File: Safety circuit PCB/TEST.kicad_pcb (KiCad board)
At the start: 2 copper layers, 100 x 50 mm, 30 parts, among them J1 430450801, J2 430450801, Q1 2N7002K, Q2 2N7002K, Q3 2N7002K, Q4 2N7002K, Q5 2N7002K, Q6 2N7002K, Q7 2N7002K

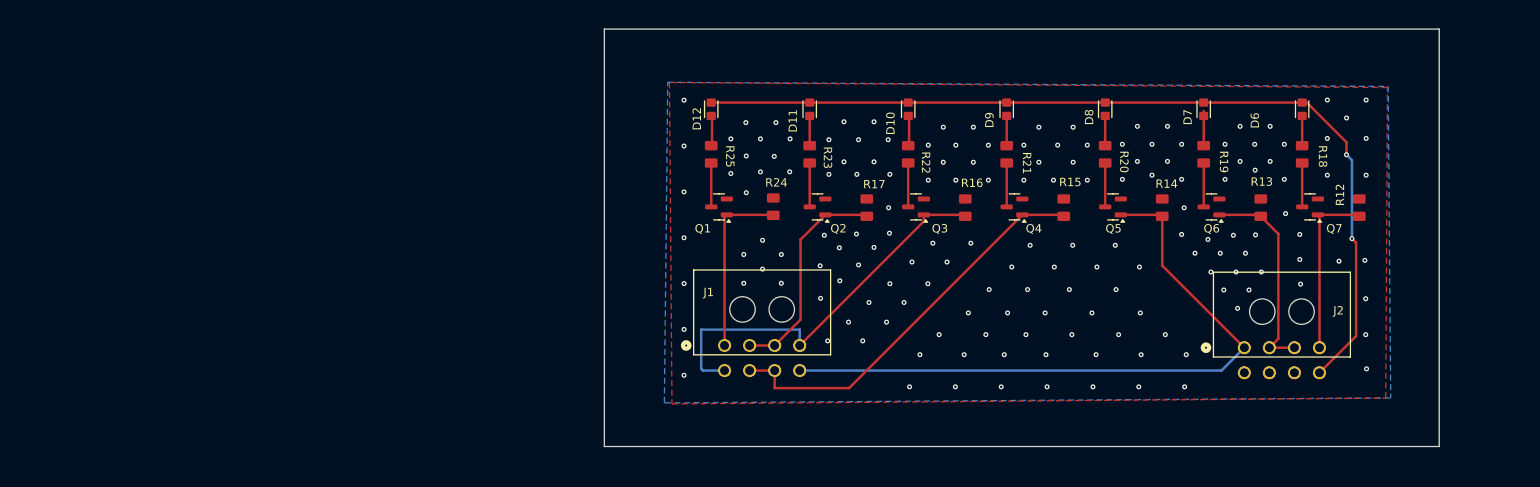
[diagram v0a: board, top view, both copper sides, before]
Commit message: Flip connectors, make more sane pin assignments for connections, get nicer tracks, and make dimensions reasonable
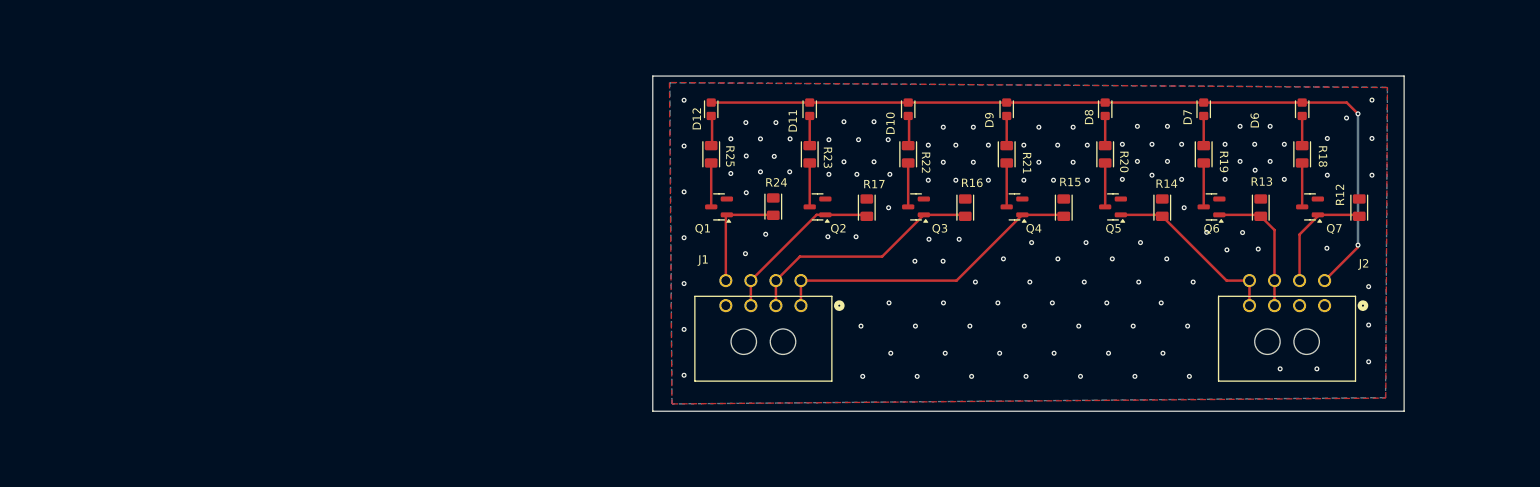
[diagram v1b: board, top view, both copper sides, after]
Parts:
- moved J2 10.9 mm to (176.3, 83.1), turned to 0 degrees
- moved J1 10.3 mm to (113.5, 83.1), turned to 0 degrees
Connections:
- J1 pad 1: /INPUT -> /INERTIA_SWITCH
- J1 pad 2: /LEFT_BUTTON -> /RIGHT_BUTTON
- J1 pad 4: /RIGHT_BUTTON -> GND
- J1 pad 5: /RIGHT_BUTTON -> /INERTIA_SWITCH
- J1 pad 6: /INERTIA_SWITCH -> /RIGHT_BUTTON
- J1 pad 7: /INERTIA_SWITCH -> /LEFT_BUTTON
- J1 pad 8: /COCKPIT_BUTTON -> /INPUT
- J2 pad 1: /COCKPIT_BUTTON -> GND
- J2 pad 2: /BOTS -> GND
- J2 pad 4: /OUTPUT -> /COCKPIT_BUTTON
- J2 pad 5: GND -> +12V
- J2 pad 6: GND -> /OUTPUT
- J2 pad 7: GND -> /BOTS
- J2 pad 8: +12V -> /COCKPIT_BUTTON
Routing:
- net /COCKPIT_BUTTON: track 79.0 -> 21.4 mm
- net /RIGHT_BUTTON: track 47.9 -> 28.8 mm
- net /INERTIA_SWITCH: track 48.2 -> 37.6 mm
- net /BOTS: track 24.8 -> 16.2 mm
- net +12V: track 108.0 -> 99.7 mm
- net /INPUT: track 21.3 -> 13.3 mm
- net /OUTPUT: track 20.8 -> 13.6 mm
- net /LEFT_BUTTON: track 26.4 -> 20.0 mm
- net GND: vias 162 -> 132
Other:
- board size 100 x 50 mm -> 90 x 40.2 mm

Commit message: Add mounting holes, round corners, add silkscreen logo and Charlie Brown
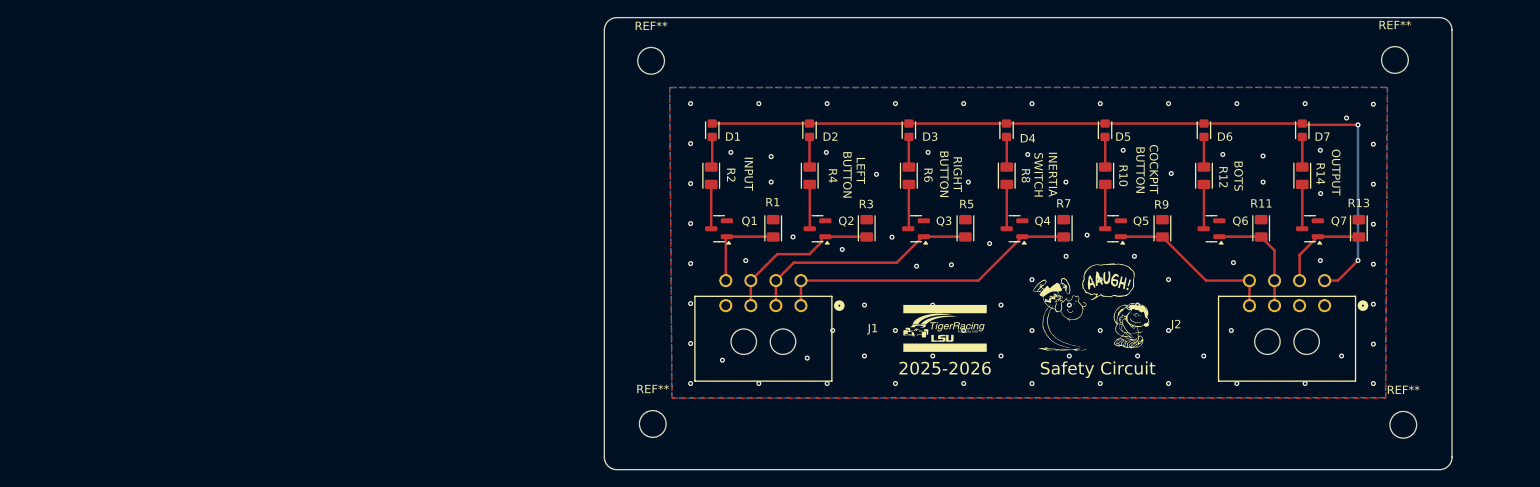
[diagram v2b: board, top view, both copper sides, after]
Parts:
- removed D10, D11, D12, D8, D9: LED, SC:HL-PSC-1608U52GC-G4
- removed R15, R16, R17, R18, R19, R20, R21, R22, R23, R24, R25: 1k, SC:CRCW0805
- added 2025-2026: LOGO, SC:tiger-racing-logo-with-name-10mm-by-5.6mm, F.Cu at (130.8, 85.9)
- added D1: LED, SC:HL-PSC-1608U52GC-G4, F.Cu at (102.9, 62.1)
- added D2: LED, SC:HL-PSC-1608U52GC-G4, F.Cu at (114.6, 62.1)
- added D3: LED, SC:HL-PSC-1608U52GC-G4, F.Cu at (126.5, 62.1)
- added D4: LED, SC:HL-PSC-1608U52GC-G4, F.Cu at (138.2, 62.1)
- added D5: LED, SC:HL-PSC-1608U52GC-G4, F.Cu at (150.0, 62.1)
- added R1: 1k, SC:CRCW0805, F.Cu at (110.2, 73.9)
- added R10: 1k, SC:CRCW0805, F.Cu at (150.0, 67.6)
- added R11: 1k, SC:CRCW0805, F.Cu at (168.7, 73.9)
- added R2: 1k, SC:CRCW0805, F.Cu at (102.8, 67.6)
- added R3: 1k, SC:CRCW0805, F.Cu at (121.4, 73.9)
- added R4: 1k, SC:CRCW0805, F.Cu at (114.6, 67.6)
- added R5: 1k, SC:CRCW0805, F.Cu at (133.2, 73.9)
- added R6: 1k, SC:CRCW0805, F.Cu at (126.5, 67.6)
- added R7: 1k, SC:CRCW0805, F.Cu at (145.0, 73.9)
- added R8: 1k, SC:CRCW0805, F.Cu at (138.2, 67.6)
- added R9: 1k, SC:CRCW0805, F.Cu at (156.8, 73.9)
- added REF**: MountingHole_3.2mm_M3, MountingHole:MountingHole_3.2mm_M3, F.Cu at (185.7, 97.4)
- added REF**: MountingHole_3.2mm_M3, MountingHole:MountingHole_3.2mm_M3, F.Cu at (95.8, 97.3)
- added REF**: MountingHole_3.2mm_M3, MountingHole:MountingHole_3.2mm_M3, F.Cu at (184.7, 53.7)
- added REF**: MountingHole_3.2mm_M3, MountingHole:MountingHole_3.2mm_M3, F.Cu at (95.6, 53.8)
- added Safety Circuit: LOGO, SC:charlie-brown-lucy-football, F.Cu at (148.3, 83.3)
- moved R12 19.0 mm to (161.8, 67.6), turned to -90 degrees
- moved R14 17.2 mm to (173.6, 67.6), turned to -90 degrees
- moved D7 12.1 mm to (173.6, 62.1)
- moved D6 12.0 mm to (161.8, 62.1)
- moved R13 12.0 mm to (180.4, 73.9)
- moved Q1 2.61 mm to (103.7, 73.9)
- moved Q2 2.61 mm to (115.5, 73.9)
- moved Q3 2.61 mm to (127.3, 73.9)
- moved Q4 2.61 mm to (139.1, 73.9)
- moved Q5 2.61 mm to (150.9, 73.9)
- moved Q6 2.61 mm to (162.7, 73.9)
- moved Q7 2.61 mm to (174.5, 73.9)
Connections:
- R12 pad 1: /OUTPUT -> Net-(D6-K)
- R12 pad 2: GND -> Net-(Q6-D)
- R13 pad 1: /BOTS -> /OUTPUT
- R14 pad 1: /COCKPIT_BUTTON -> Net-(D7-K)
- R14 pad 2: GND -> Net-(Q7-D)
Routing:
- net Net-(D1-K): track 0.00 -> 3.66 mm
- net Net-(D5-K): track 0.00 -> 3.62 mm
- net Net-(D2-K): track 0.00 -> 3.62 mm
- net Net-(D4-K): track 0.00 -> 3.62 mm
- net Net-(D3-K): track 0.00 -> 3.61 mm
- net Net-(D9-K): track 3.56 -> 0.00 mm
- net Net-(D8-K): track 3.56 -> 0.00 mm
- net Net-(D12-K): track 3.56 -> 0.00 mm
- net Net-(D11-K): track 3.56 -> 0.00 mm
- net Net-(D10-K): track 3.56 -> 0.00 mm
- net /INPUT: track 13.3 -> 10.6 mm
- net /OUTPUT: track 13.6 -> 11.0 mm
- net /BOTS: track 16.2 -> 13.7 mm
- net /LEFT_BUTTON: track 20.0 -> 18.8 mm
- net /RIGHT_BUTTON: track 28.8 -> 27.6 mm
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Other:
- board size 90 x 40.2 mm -> 101.5 x 54.2 mm
- board text added: "BOTS"
- board text added: "BUTTON"
- board text added: "COCKPIT"
- board text added: "INERTIA"
- board text added: "INPUT"
- board text added: "LEFT"
- board text added: "OUTPUT"
- board text added: "RIGHT"
- board text added: "SWITCH"

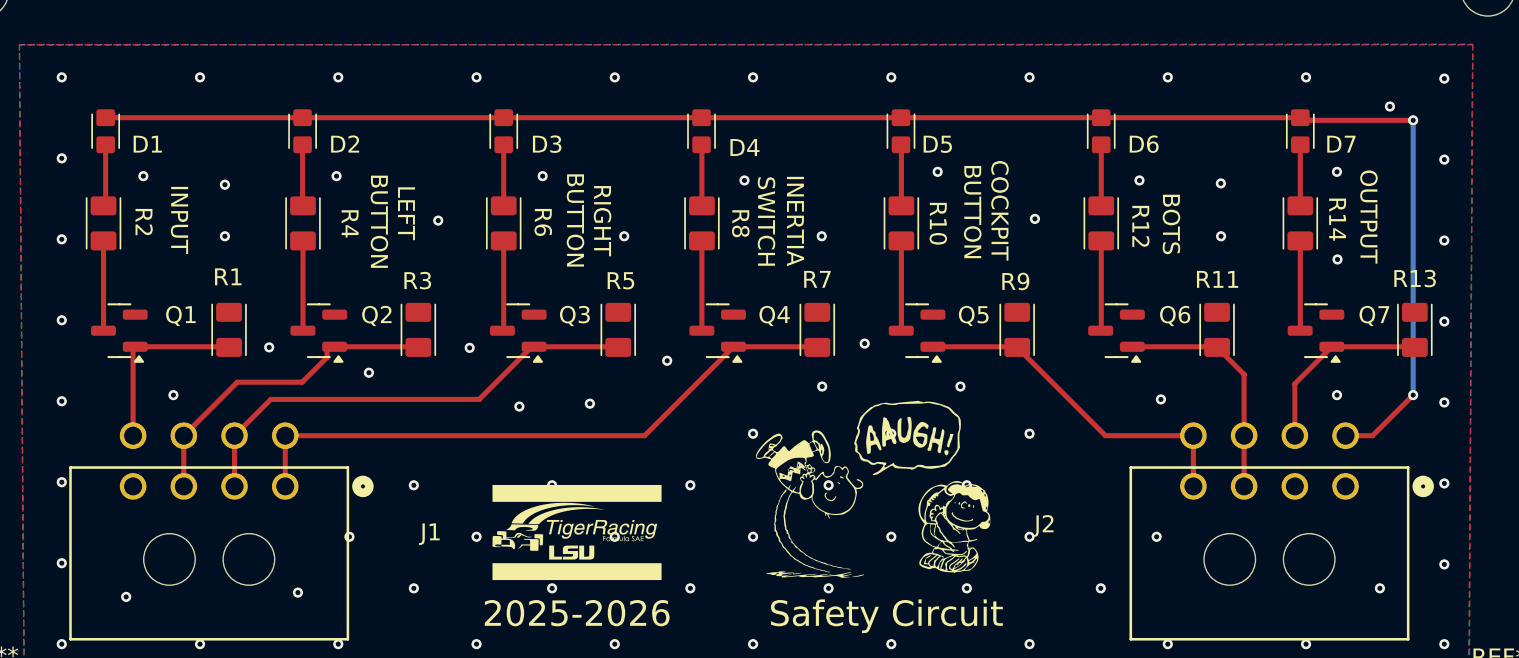
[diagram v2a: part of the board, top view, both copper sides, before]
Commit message: Implement improvement advice from Jacob
Add ground vias next to all NMOS grounds

Change pull-down resistors at gates of NMOS to 100k from 1k, and change datasheet and resistor fields (part #, JLC Part #, etc...) accordingly

Make 12V power track 0.5 mm from 0.3mm

Add falstad simulation text file to Safety Circuit project

ERC and DRC still all pass
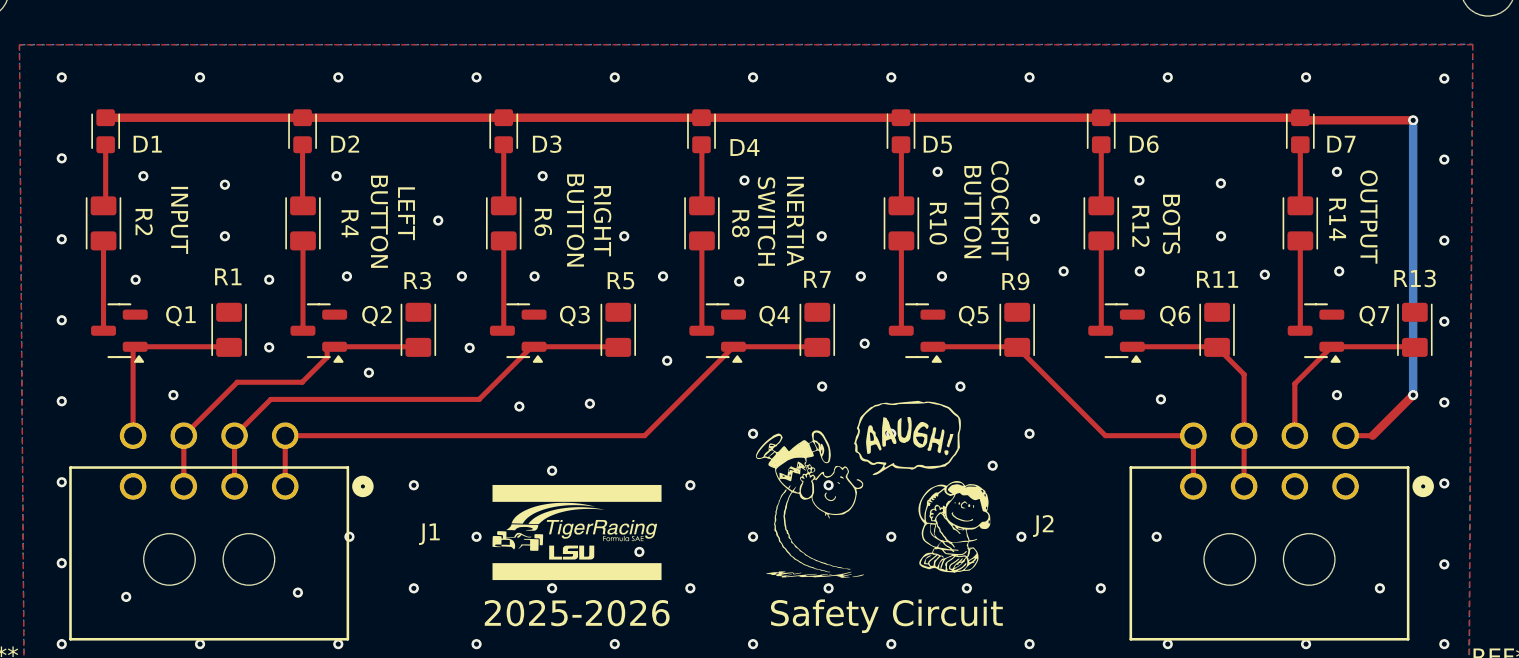
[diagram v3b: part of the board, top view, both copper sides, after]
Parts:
- R1, R11, R13, R3, R5, R7, R9: value 1k -> 100k
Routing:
- net GND: vias 87 -> 98
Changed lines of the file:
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@@
 			)
 		)
-		(property "Value" "1k"
+		(property "Value" "100k"
 			(at -3.172 0.011 0)
 			(unlocked yes)
@@
 			)
 		)
-		(property "Datasheet" "https://jlcpcb.com/api/file/downloadByFileSystemAccessId/8588950168741404672"
+		(property "Datasheet" "https://jlcpcb.com/api/file/downloadByFileSystemAccessId/8590171393792389120"
 			(at 0 0 90)
 			(unlocked yes)
@@
 			)
 		)
-		(property "Digikey" "https://www.digikey.com/en/products/detail/vishay-dale/CRCW08051K00FKEA/1175637"
+		(property "Digikey" "https://www.digikey.com/en/products/detail/vishay-dale/CRCW0805100KJNEA/1175246"
 			(at 0 0 90)
 			(unlocked yes)
@@
 			)
 		)
-		(property "MFR Part #" "CRCW08051K00FKEA"
+		(property "MFR Part #" "CRCW0805100KJNEA"
 			(at 0 0 90)
 			(unlocked yes)
@@
 			)
 		)
-		(property "Value" "1k"
+		(property "Value" "100k"
 			(at -3.172 0.1 0)
 			(unlocked yes)
@@
 			)
 		)
-		(property "Datasheet" "https://jlcpcb.com/api/file/downloadByFileSystemAccessId/8588950168741404672"
+		(property "Datasheet" "https://jlcpcb.com/api/file/downloadByFileSystemAccessId/8590171393792389120"
 			(at 0 0 90)
 			(unlocked yes)
@@
 			)
 		)
-		(property "Digikey" "https://www.digikey.com/en/products/detail/vishay-dale/CRCW08051K00FKEA/1175637"
+		(property "Digikey" "https://www.digikey.com/en/products/detail/vishay-dale/CRCW0805100KJNEA/1175246"
 			(at 0 0 90)
 			(unlocked yes)
@@
 			)
 		)
-		(property "MFR Part #" "CRCW08051K00FKEA"
+		(property "MFR Part #" "CRCW0805100KJNEA"
 			(at 0 0 90)
 			(unlocked yes)
@@
 			)
 		)
-		(property "Value" "1k"
+		(property "Value" "100k"
 			(at -2.918 0.122 0)
 			(unlocked yes)
@@
 			)
 		)
-		(property "Datasheet" "https://jlcpcb.com/api/file/downloadByFileSystemAccessId/8588950168741404672"
+		(property "Datasheet" "https://jlcpcb.com/api/file/downloadByFileSystemAccessId/8590171393792389120"
 			(at 0 0 90)
 			(unlocked yes)
@@
 			)
 		)
-		(property "Digikey" "https://www.digikey.com/en/products/detail/vishay-dale/CRCW08051K00FKEA/1175637"
+		(property "Digikey" "https://www.digikey.com/en/products/detail/vishay-dale/CRCW0805100KJNEA/1175246"
 			(at 0 0 90)
 			(unlocked yes)
@@
 			)
 		)
-		(property "MFR Part #" "CRCW08051K00FKEA"
+		(property "MFR Part #" "CRCW0805100KJNEA"
 			(at 0 0 90)
 			(unlocked yes)
@@
 			)
 		)
-		(property "Value" "1k"
+		(property "Value" "100k"
 			(at -2.918 0.235 0)
 			(unlocked yes)
@@
 			)
 		)
-		(property "Datasheet" "https://jlcpcb.com/api/file/downloadByFileSystemAccessId/8588950168741404672"
+		(property "Datasheet" "https://jlcpcb.com/api/file/downloadByFileSystemAccessId/8590171393792389120"
 			(at 0 0 90)
 			(unlocked yes)
@@
 			)
 		)
-		(property "Digikey" "https://www.digikey.com/en/products/detail/vishay-dale/CRCW08051K00FKEA/1175637"
+		(property "Digikey" "https://www.digikey.com/en/products/detail/vishay-dale/CRCW0805100KJNEA/1175246"
 			(at 0 0 90)
 			(unlocked yes)
@@
 			)
 		)
-		(property "MFR Part #" "CRCW08051K00FKEA"
+		(property "MFR Part #" "CRCW0805100KJNEA"
 			(at 0 0 90)
 			(unlocked yes)
@@
 			)
 		)
-		(property "Value" "1k"
+		(property "Value" "100k"
 			(at -2.918 -0.013 0)
 			(unlocked yes)
@@
 			)
 		)
-		(property "Datasheet" "https://jlcpcb.com/api/file/downloadByFileSystemAccessId/8588950168741404672"
+		(property "Datasheet" "https://jlcpcb.com/api/file/downloadByFileSystemAccessId/8590171393792389120"
 			(at 0 0 90)
 			(unlocked yes)
@@
 			)
 		)
-		(property "Digikey" "https://www.digikey.com/en/products/detail/vishay-dale/CRCW08051K00FKEA/1175637"
+		(property "Digikey" "https://www.digikey.com/en/products/detail/vishay-dale/CRCW0805100KJNEA/1175246"
 			(at 0 0 90)
 			(unlocked yes)
@@
 			)
 		)
-		(property "MFR Part #" "CRCW08051K00FKEA"
+		(property "MFR Part #" "CRCW0805100KJNEA"
 			(at 0 0 90)
 			(unlocked yes)
@@
 			)
 		)
-		(property "Value" "1k"
-			(at -2.918 0.009 180)
+		(property "Value" "100k"
+			(at -2.918 0.009 0)
 			(unlocked yes)
 			(layer "F.Fab")
@@
 			)
 		)
-		(property "Datasheet" "https://jlcpcb.com/api/file/downloadByFileSystemAccessId/8588950168741404672"
+		(property "Datasheet" "https://jlcpcb.com/api/file/downloadByFileSystemAccessId/8590171393792389120"
 			(at 0 0 90)
 			(unlocked yes)
@@
 			)
 		)
-		(property "Digikey" "https://www.digikey.com/en/products/detail/vishay-dale/CRCW08051K00FKEA/1175637"
+		(property "Digikey" "https://www.digikey.com/en/products/detail/vishay-dale/CRCW0805100KJNEA/1175246"
 			(at 0 0 90)
 			(unlocked yes)
@@
 			)
 		)
-		(property "MFR Part #" "CRCW08051K00FKEA"
+		(property "MFR Part #" "CRCW0805100KJNEA"
 			(at 0 0 90)
 			(unlocked yes)
@@
 			)
 		)
-		(property "Value" "1k"
+		(property "Value" "100k"
 			(at -2.918 -0.035 0)
 			(unlocked yes)
@@
 			)
 		)
-		(property "Datasheet" "https://jlcpcb.com/api/file/downloadByFileSystemAccessId/8588950168741404672"
+		(property "Datasheet" "https://jlcpcb.com/api/file/downloadByFileSystemAccessId/8590171393792389120"
 			(at 0 0 90)
 			(unlocked yes)
@@
 			)
 		)
-		(property "Digikey" "https://www.digikey.com/en/products/detail/vishay-dale/CRCW08051K00FKEA/1175637"
+		(property "Digikey" "https://www.digikey.com/en/products/detail/vishay-dale/CRCW0805100KJNEA/1175246"
 			(at 0 0 90)
 			(unlocked yes)
@@
 			)
 		)
-		(property "MFR Part #" "CRCW08051K00FKEA"
+		(property "MFR Part #" "CRCW0805100KJNEA"
 			(at 0 0 90)
 			(unlocked yes)
@@
 		(start 180.275 61.468)
 		(end 173.754 61.468)
-		(width 0.3)
+		(width 0.5)
 		(layer "F.Cu")
 		(net 2)
@@
 		(start 126.475 61.314)
 		(end 114.575 61.314)
-		(width 0.3)
+		(width 0.5)
 		(layer "F.Cu")
 		(net 2)
@@
 		(start 161.820833 61.314)
 		(end 149.975 61.314)
-		(width 0.3)
+		(width 0.5)
 		(layer "F.Cu")
 		(net 2)
@@
 		(start 177.873999 80.125001)
 		(end 180.275 77.724)
-		(width 0.3)
+		(width 0.5)
 		(layer "F.Cu")
 		(net 2)
@@
 		(start 138.175 61.314)
 		(end 126.475 61.314)
-		(width 0.3)
+		(width 0.5)
 		(layer "F.Cu")
 		(net 2)
@@
 		(start 114.575 61.314)
 		(end 102.925 61.314)
-		(width 0.3)
+		(width 0.5)
 		(layer "F.Cu")
 		(net 2)
@@
 		(start 173.6 61.314)
 		(end 161.820833 61.314)
-		(width 0.3)
+		(width 0.5)
 		(layer "F.Cu")
 		(net 2)
@@
 		(start 149.975 61.314)
 		(end 138.175 61.314)
-		(width 0.3)
+		(width 0.5)
 		(layer "F.Cu")
 		(net 2)
@@
 		(start 180.275 61.468)
 		(end 180.275 77.724)
-		(width 0.3)
+		(width 0.5)
 		(layer "B.Cu")
 		(net 2)
@@
 	)
 	(via
+		(at 147.6 70.7)
+		(size 0.6)
+		(drill 0.3)
+		(layers "F.Cu" "B.Cu")
+		(free yes)
+		(net 6)
+	)
+	(via
 		(at 124.8664 58.928)
 		(size 0.6)
@@
 	)
 	(via
-		(at 178.9 60.65)
+		(at 112.6 70.9)
+		(size 0.6)
+		(drill 0.3)
+		(layers "F.Cu" "B.Cu")
+		(free yes)
+		(net 6)
+	)
+	(via
+		(at 152.4 70.7)
 		(size 0.6)
 		(drill 0.3)
@@
 	)
 	(via
-		(at 175.8 69.7)
+		(at 175.9 70.4)
 		(size 0.6)
 		(drill 0.3)
@@
 	)
 	(via
+		(at 104.7 70.9)
+		(size 0.6)
+		(drill 0.3)
+		(layers "F.Cu" "B.Cu")
+		(free yes)
+		(net 6)
+	)
+	(via
 		(at 100.33 78.086857)
 		(size 0.6)
@@
 	)
 	(via
+		(at 171.5 70.6)
+		(size 0.6)
+		(drill 0.3)
+		(layers "F.Cu" "B.Cu")
+		(free yes)
+		(net 6)
+	)
+	(via
+		(at 128.3 70.7)
+		(size 0.6)
+		(drill 0.3)
+		(layers "F.Cu" "B.Cu")
+		(free yes)
+		(net 6)
+	)
+	(via
 		(at 149.4028 80.01)
 		(size 0.6)
@@
 	)
 	(via
+		(at 140.4 71)
+		(size 0.6)
+		(drill 0.3)
+		(layers "F.Cu" "B.Cu")
+		(free yes)
+		(net 6)
+	)
+	(via
 		(at 175.768 64.516)
 		(size 0.6)
@@
 	)
 	(via
-		(at 153.8732 83.058)
+		(at 155.4 81.9)
 		(size 0.6)
 		(drill 0.3)
@@
 	)
 	(via
+		(at 135.9 70.7)
+		(size 0.6)
+		(drill 0.3)
+		(layers "F.Cu" "B.Cu")
+		(free yes)
+		(net 6)
+	)
+	(via
 		(at 141.224 80.01)
 		(size 0.6)
@@
 	)
 	(via
+		(at 117.2 70.7)
+		(size 0.6)
+		(drill 0.3)
+		(layers "F.Cu" "B.Cu")
+		(free yes)
+		(net 6)
+	)
+	(via
 		(at 168.91 68.326)
 		(size 0.6)
@@
 	)
 	(via
+		(at 124 70.7)
+		(size 0.6)
+		(drill 0.3)
+		(layers "F.Cu" "B.Cu")
+		(free yes)
+		(net 6)
+	)
+	(via
+		(at 164.1 70.4)
+		(size 0.6)
+		(drill 0.3)
+		(layers "F.Cu" "B.Cu")
+		(free yes)
+		(net 6)
+	)
+	(via
 		(at 121.158 89.154)
 		(size 0.6)
@@
 	)
 	(via
-		(at 133.0452 86.106)
+		(at 134.5 87)
 		(size 0.6)
 		(drill 0.3)
@@
 	)
 	(via
-		(at 157.5816 86.106)
+		(at 157.1 86.106)
 		(size 0.6)
 		(drill 0.3)
@@
 	)
 	(via
-		(at 129.3368 83.058)
+		(at 159.6 70.4)
+		(size 0.6)
+		(drill 0.3)
+		(layers "F.Cu" "B.Cu")
+		(free yes)
+		(net 6)
+	)
+	(via
+		(at 129.3368 82.2)
 		(size 0.6)
 		(drill 0.3)
